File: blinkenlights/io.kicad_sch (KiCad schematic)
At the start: 11 parts, among them J501 Conn_02x10_Odd_Even, U501 XRA1403, U502 PCA9306DP

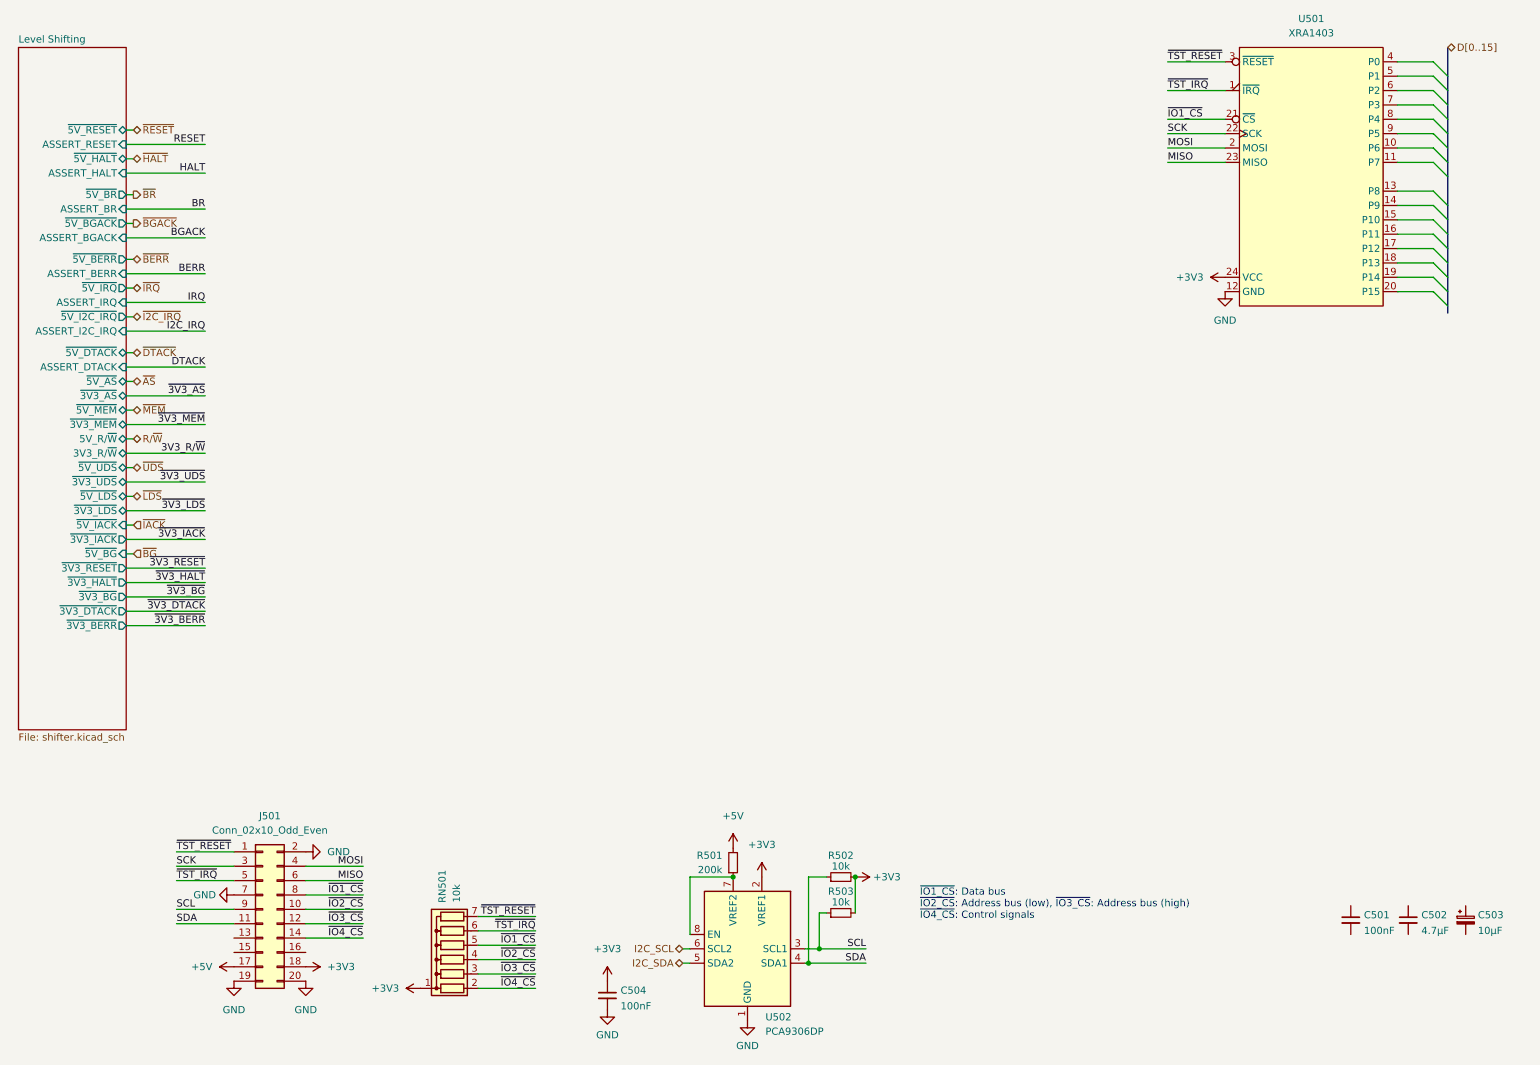
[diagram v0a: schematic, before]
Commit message: Get rid of CPU on blinkenlights board
- We don't really care for having a full processor chilling on this
  board more than we do about being able to do a few bus transactions
  (to do fun stuff like flashing the boot ROMs) so we're going to put a
  bunch of SPI IO expanders instead; this should allow us to somewhat
  recreate bus cycles.

  We'll have to implement the run/halt/single step controls with
  dedicated logic though.
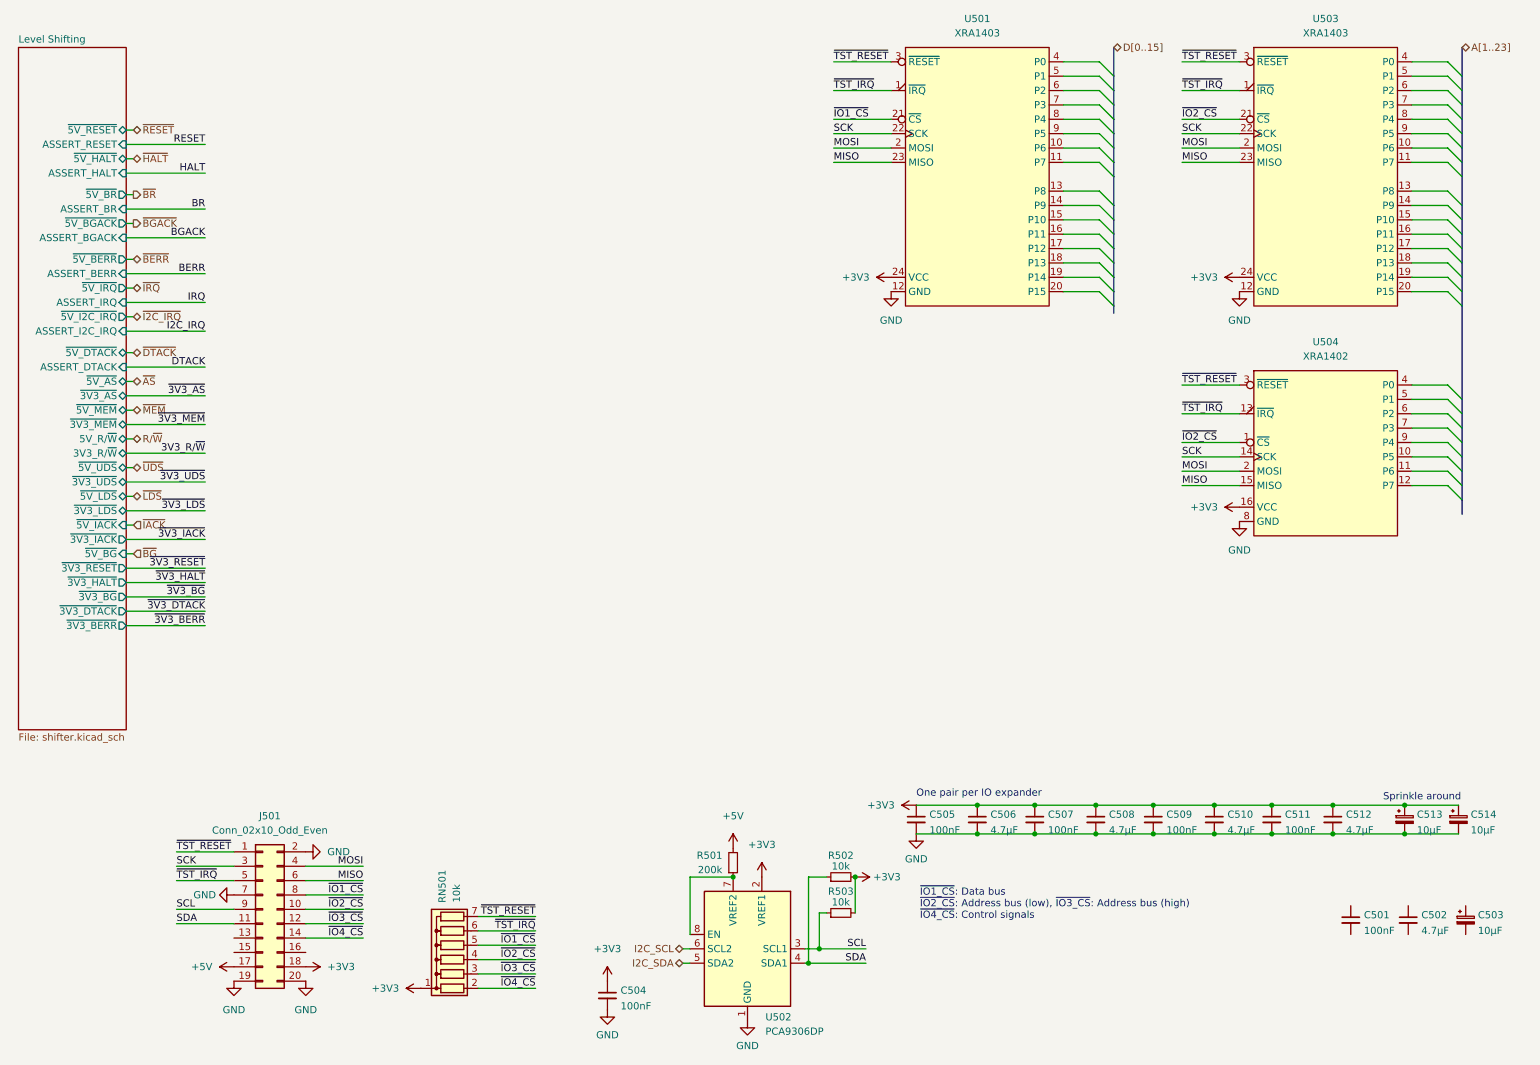
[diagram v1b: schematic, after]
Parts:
- added C505, C507, C509, C511: 100nF, Capacitor_SMD:C_0805_2012Metric, symbol Device:C_Small
- added C506, C508, C510, C512: 4.7µF, Capacitor_SMD:C_0805_2012Metric, symbol Device:C_Small
- added C513, C514: 10µF, Capacitor_Tantalum_SMD:CP_EIA-3528-21_Kemet-B, symbol Device:C_Polarized_Small
- added U503: XRA1403, Package_SO:TSSOP-24_4.4x7.8mm_P0.65mm, symbol 68komputer-common:XRA1403
- added U504: XRA1402, Package_SO:TSSOP-16_4.4x5mm_P0.65mm, symbol 68komputer-common:XRA1402
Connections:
- net +3V3: now also C505.1, C506.1, C507.1, C508.1, C509.1, C510.1, C511.1, C512.1, C513.1, C514.1, U503.24 (VCC), U504.16 (VCC)
- net GND: now also C505.2, C506.2, C507.2, C508.2, C509.2, C510.2, C511.2, C512.2, C513.2, C514.2, U503.12 (GND), U504.8 (GND)
- net MISO: now also U503.23 (MISO), U504.15 (MISO)
- net MOSI: now also U503.2 (MOSI), U504.2 (MOSI)
- net SCK: now also U503.22 (SCK), U504.14 (SCK)
- net ~{IO2_CS}: now also U503.21 (~{CS}), U504.1 (~{CS})
- net ~{TST_IRQ}: now also U503.1 (~{IRQ}), U504.13 (~{IRQ})
- net ~{TST_RESET}: now also U503.3 (~{RESET}), U504.3 (~{RESET})
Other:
- note added: "One pair per IO expander"
- note added: "Sprinkle around"
- moved on the sheet: U501

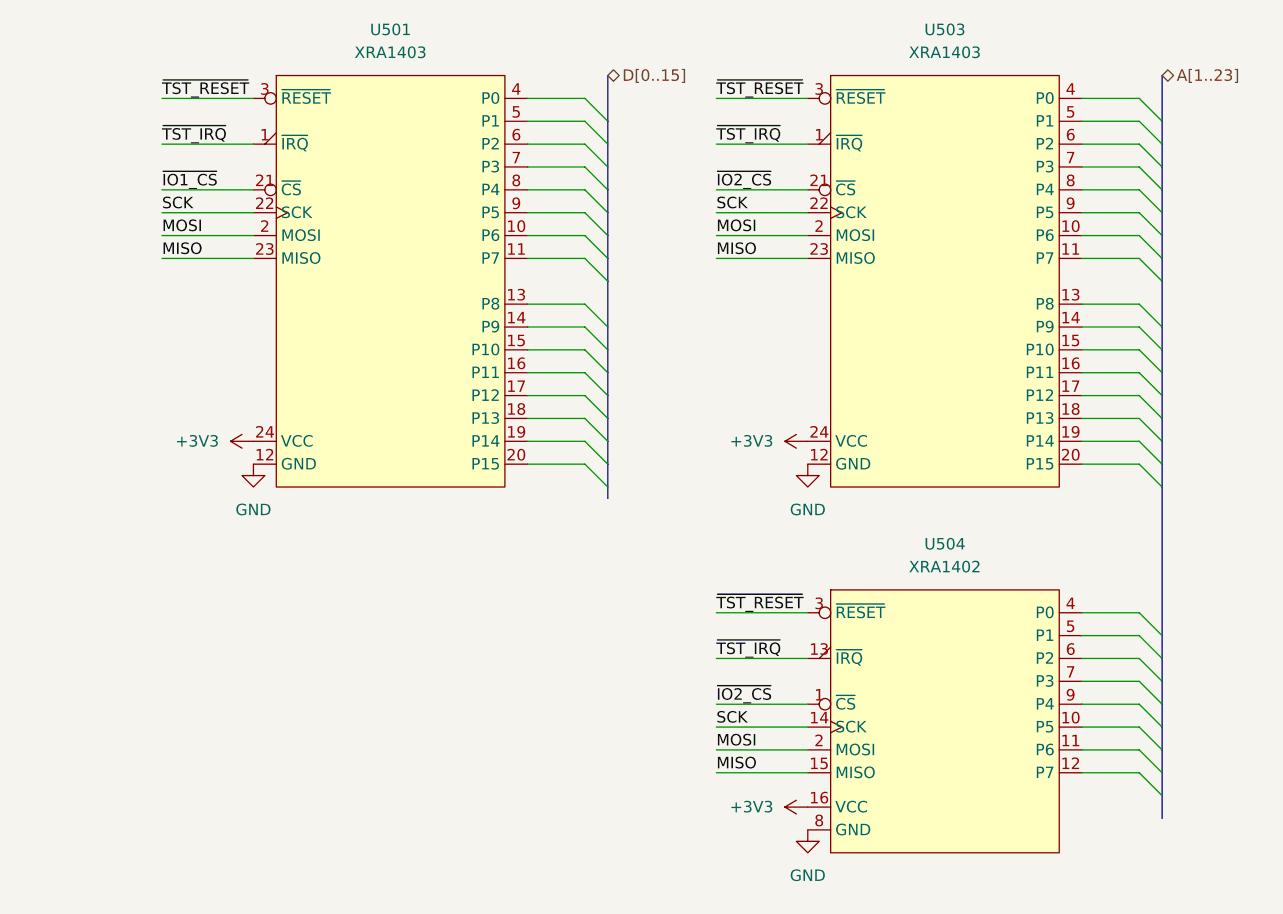
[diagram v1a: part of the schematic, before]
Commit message: Connected data/address bus to expanders
- Finished routing the remaining address and data lines to the SPI IO
  expanders, which are used externally to control the bus. Also removed
  some superfluous level shifters
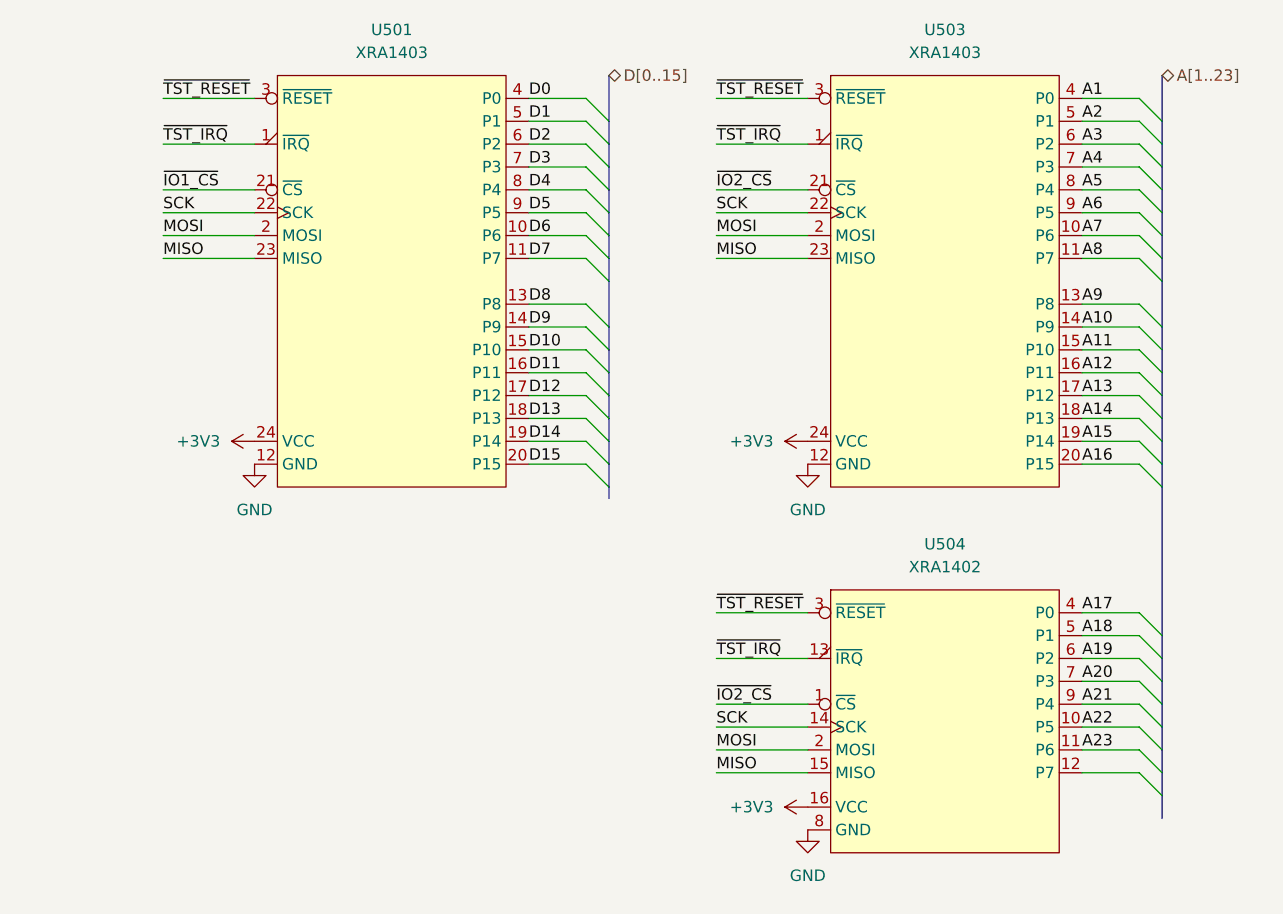
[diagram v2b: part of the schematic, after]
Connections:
- net A7: now reaches U503.10 (P6)
- net A8: now reaches U503.11 (P7)
- net A9: now reaches U503.13 (P8)
- net A10: now reaches U503.14 (P9)
- net A11: now reaches U503.15 (P10)
- net A12: now reaches U503.16 (P11)
- net A13: now reaches U503.17 (P12)
- net A14: now reaches U503.18 (P13)
- net A15: now reaches U503.19 (P14)
- net A16: now reaches U503.20 (P15)
- net A1: now reaches U503.4 (P0)
- net A2: now reaches U503.5 (P1)
- net A3: now reaches U503.6 (P2)
- net A4: now reaches U503.7 (P3)
- net A5: now reaches U503.8 (P4)
- net A6: now reaches U503.9 (P5)
- net D6: now reaches U501.10 (P6)
- net D7: now reaches U501.11 (P7)
- net D8: now reaches U501.13 (P8)
- net D9: now reaches U501.14 (P9)
- net D10: now reaches U501.15 (P10)
- net D11: now reaches U501.16 (P11)
- net D12: now reaches U501.17 (P12)
- net D13: now reaches U501.18 (P13)
- net D14: now reaches U501.19 (P14)
- net D15: now reaches U501.20 (P15)
- net D0: now reaches U501.4 (P0)
- net D1: now reaches U501.5 (P1)
- net D2: now reaches U501.6 (P2)
- net D3: now reaches U501.7 (P3)
- net D4: now reaches U501.8 (P4)
- net D5: now reaches U501.9 (P5)
- net A22: now reaches U504.10 (P5)
- net A23: now reaches U504.11 (P6)
- net A17: now reaches U504.4 (P0)
- net A18: now reaches U504.5 (P1)
- net A19: now reaches U504.6 (P2)
- net A20: now reaches U504.7 (P3)
- net A21: now reaches U504.9 (P4)
